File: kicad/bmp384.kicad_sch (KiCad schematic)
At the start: 3 parts, among them U901 BMP384

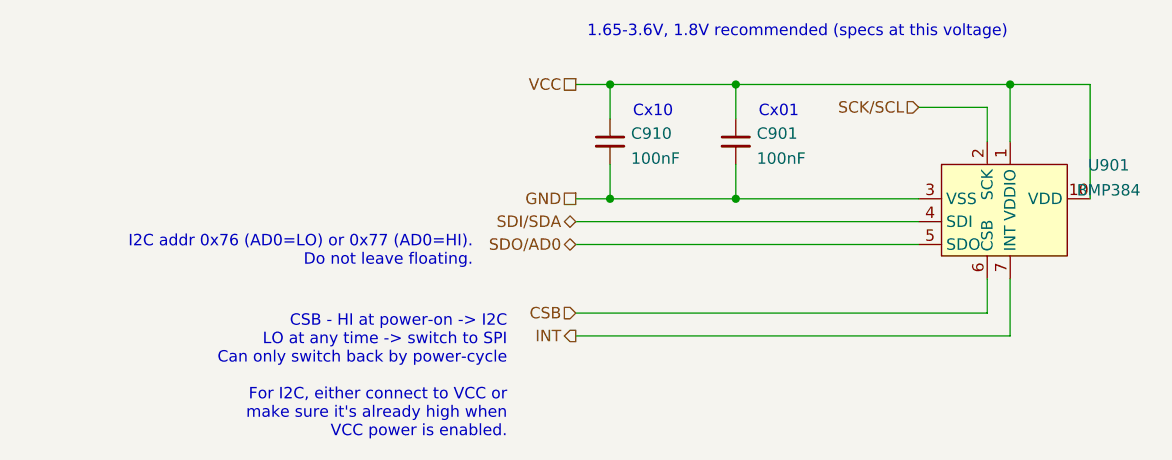
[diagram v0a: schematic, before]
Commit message: Broke down sensor block into a tree of sheets
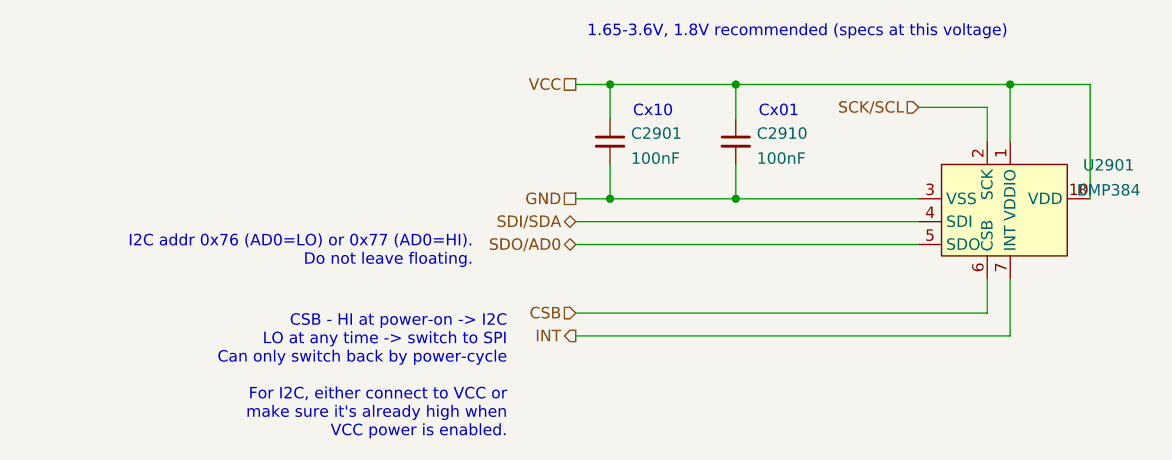
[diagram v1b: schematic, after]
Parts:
- renumbered C910 to C2901, C901 to C2910, U901 to U2901
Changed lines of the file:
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@@
   (symbol (lib_id "KwanSystems:BMP384") (at 137.16 91.44 0)
     (in_bom yes) (on_board yes) (fields_autoplaced)
-    (property "Reference" "U901" (id 0) (at 148.1106 85.1748 0))
+    (property "Reference" "U2901" (id 0) (at 148.1106 85.1748 0))
     (property "Value" "BMP384" (id 1) (at 148.1106 87.9499 0))
     (property "Footprint" "KwanSystems:BMP384" (id 2) (at 137.16 91.44 0)
@@
   (symbol (lib_id "Device:C_Small") (at 92.71 82.55 0)
     (in_bom yes) (on_board yes) (fields_autoplaced)
-    (property "Reference" "C910" (id 0) (at 95.0341 81.6478 0)
+    (property "Reference" "C2901" (id 0) (at 95.0341 81.6478 0)
       (effects (font (size 1.27 1.27)) (justify left))
     )
@@
   (symbol (lib_id "Device:C_Small") (at 106.68 82.55 0)
     (in_bom yes) (on_board yes) (fields_autoplaced)
-    (property "Reference" "C901" (id 0) (at 109.0041 81.6478 0)
+    (property "Reference" "C2910" (id 0) (at 109.0041 81.6478 0)
       (effects (font (size 1.27 1.27)) (justify left))
     )

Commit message: One shining moment
Commit board while it still works
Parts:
- C2901, C2910: Digikey (none) -> 399-C0402C104K4RAC7411CT-ND
- U2901: Digikey (none) -> 828-BMP384CT-ND; Purpose (none) -> Pressure sensor
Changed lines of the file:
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@@
+      (effects (font (size 1.27 1.27)) hide)
+    )
+    (property "Digikey" "828-BMP384CT-ND" (id 4) (at 137.16 91.44 0)
+      (effects (font (size 1.27 1.27)) hide)
+    )
+    (property "Purpose" "Pressure sensor" (id 5) (at 137.16 91.44 0)
       (effects (font (size 1.27 1.27)) hide)
     )
@@
       (effects (font (size 1.27 1.27)) hide)
     )
+    (property "Digikey" "399-C0402C104K4RAC7411CT-ND" (id 4) (at 92.71 82.55 0)
+      (effects (font (size 1.27 1.27)) hide)
+    )
     (pin "1")
     (pin "2")
@@
       (effects (font (size 1.27 1.27)) hide)
     )
+    (property "Digikey" "399-C0402C104K4RAC7411CT-ND" (id 4) (at 106.68 82.55 0)
+      (effects (font (size 1.27 1.27)) hide)
+    )

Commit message: Added a purpose field to bypass capacitors
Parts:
- C2901: Purpose (none) -> BMP VDD bypass
- C2910: Purpose (none) -> BMP VDDIO bypass
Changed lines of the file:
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@@
+      (effects (font (size 1.27 1.27)) hide)
+    )
+    (property "Purpose" "BMP VDD bypass" (id 5) (at 92.71 82.55 0)
       (effects (font (size 1.27 1.27)) hide)
     )
@@
       (effects (font (size 1.27 1.27)) hide)
     )
+    (property "Purpose" "BMP VDDIO bypass" (id 5) (at 106.68 82.55 0)
+      (effects (font (size 1.27 1.27)) hide)
+    )

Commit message: Checkin before branch
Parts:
- renumbered C2910 to C1901, C2901 to C1910, U2901 to U1901
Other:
- company: (none) -> Kwan Systems
- title: (none) -> Rollercoasterometer
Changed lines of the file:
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@@
 (kicad_sch (version 20211123) (generator eeschema)
-  (paper "A4")
+  (paper "USLetter")
+  (title_block
+    (title "Rollercoasterometer")
+    (date "2022-10-07")
+    (company "Kwan Systems")
+  )
   (junction (at 92.71 76.2) (diameter 0) (color 0 0 0 0)
   )
@@
     (effects (font (size 1.27 1.27)) (justify right))
   )
-  (symbol (lib_id "KwanSystems:BMP384") (at 137.16 91.44 0)
+  (symbol (lib_id "KwanSystems:BMP384") (at 137.16 91.44 0) (unit 1)
     (in_bom yes) (on_board yes) (fields_autoplaced)
-    (property "Reference" "U2901" (id 0) (at 148.1106 85.1748 0))
-    (property "Value" "BMP384" (id 1) (at 148.1106 87.9499 0))
+    (property "Reference" "U1901" (id 0) (at 148.1106 85.4416 0))
+    (property "Value" "BMP384" (id 1) (at 148.1106 87.9785 0))
     (property "Footprint" "KwanSystems:BMP384" (id 2) (at 137.16 91.44 0)
       (effects (font (size 1.27 1.27)) hide)
@@
     (pin "9")
   )
-  (symbol (lib_id "Device:C_Small") (at 92.71 82.55 0)
+  (symbol (lib_id "Device:C_Small") (at 92.71 82.55 0) (unit 1)
     (in_bom yes) (on_board yes) (fields_autoplaced)
-    (property "Reference" "C2901" (id 0) (at 95.0341 81.6478 0)
+    (property "Reference" "C1910" (id 0) (at 95.0341 81.7216 0)
       (effects (font (size 1.27 1.27)) (justify left))
     )
-    (property "Value" "100nF" (id 1) (at 95.0341 84.4229 0)
+    (property "Value" "100nF" (id 1) (at 95.0341 84.2585 0)
       (effects (font (size 1.27 1.27)) (justify left))
     )
@@
     (pin "2")
   )
-  (symbol (lib_id "Device:C_Small") (at 106.68 82.55 0)
+  (symbol (lib_id "Device:C_Small") (at 106.68 82.55 0) (unit 1)
     (in_bom yes) (on_board yes) (fields_autoplaced)
-    (property "Reference" "C2910" (id 0) (at 109.0041 81.6478 0)
+    (property "Reference" "C1901" (id 0) (at 109.0041 81.7216 0)
       (effects (font (size 1.27 1.27)) (justify left))
     )
-    (property "Value" "100nF" (id 1) (at 109.0041 84.4229 0)
+    (property "Value" "100nF" (id 1) (at 109.0041 84.2585 0)
       (effects (font (size 1.27 1.27)) (justify left))
     )
